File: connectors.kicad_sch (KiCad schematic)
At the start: 9 parts

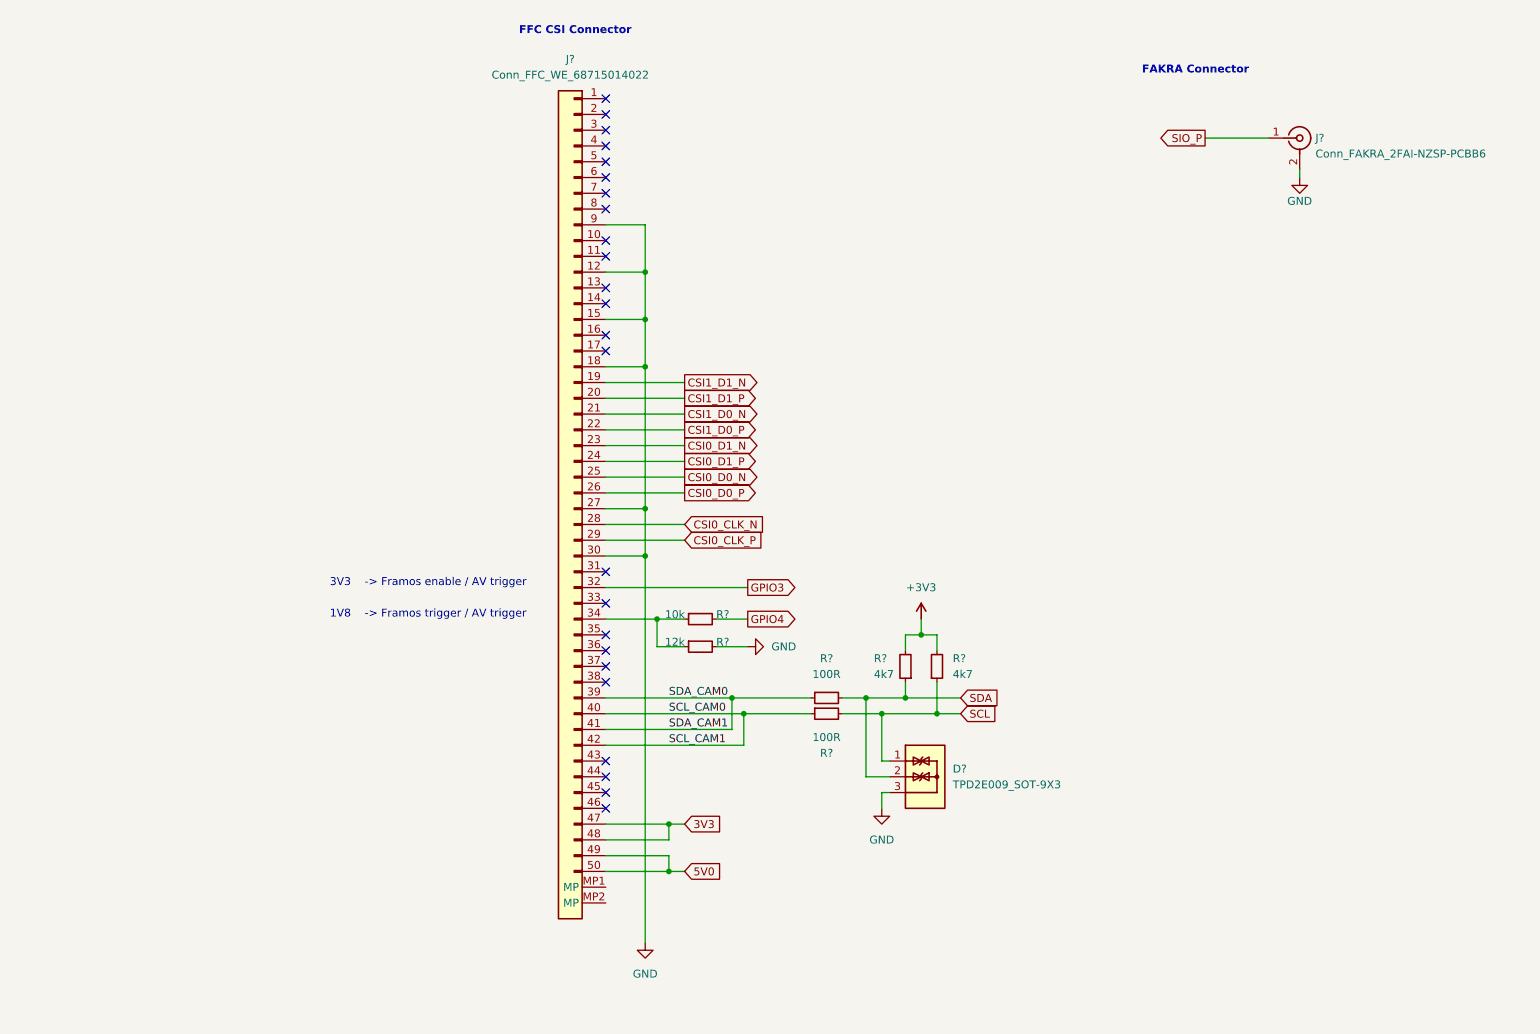
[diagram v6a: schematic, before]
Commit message: Anotate components and fix ERC errors and warnings
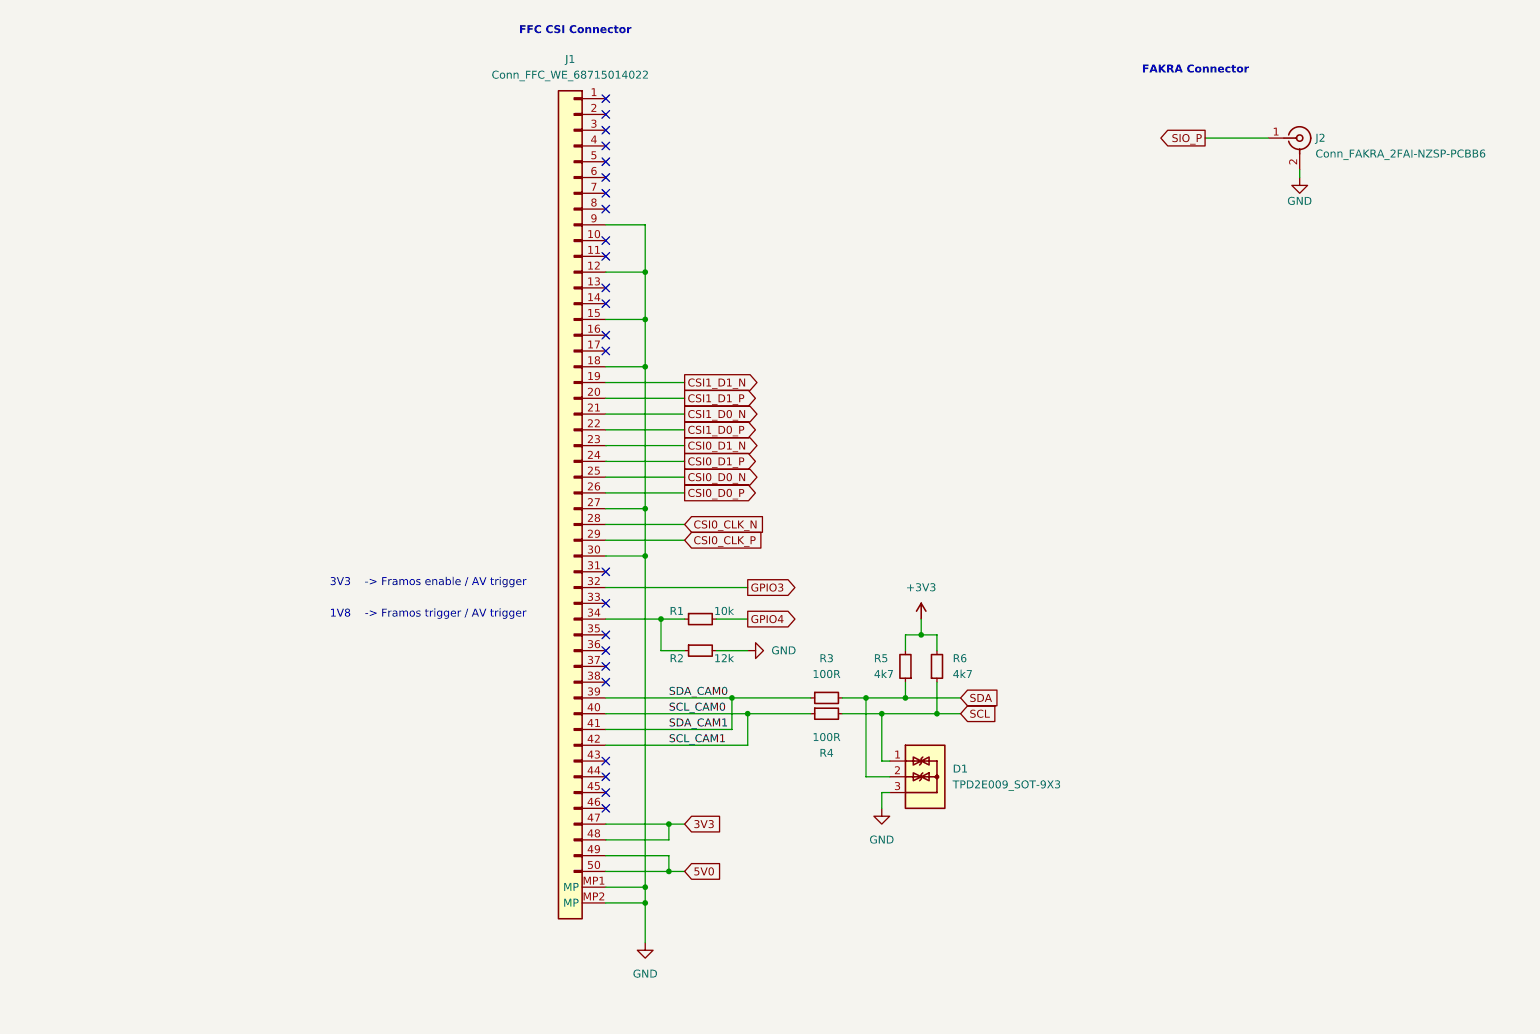
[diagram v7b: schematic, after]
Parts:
- removed R?: R_10k_0402, framos-csi-adapter-footprints:R_0402_1005Metric, symbol framos-csi-adapter:R_10k_0402
- removed R?: R_12k_0402, framos-csi-adapter-footprints:R_0402_1005Metric, symbol framos-csi-adapter:R_12k_0402
- added R1: R_10k_0402, antmicro-footprints:R_0402_1005Metric, symbol antmicroResistors0402:R_10k_0402
- added R2: R_12k_0402, antmicro-footprints:R_0402_1005Metric, symbol antmicroResistors0402:R_12k_0402
- gave numbers to parts that had none: 7
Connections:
- net GND: now also J1.MP1 (MP), J1.MP2 (MP), R2.2
- net GPIO4: now also R1.2
- net at J1.34: now also R1.1, R2.1

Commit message: Implement changes suggested in design review to schematics
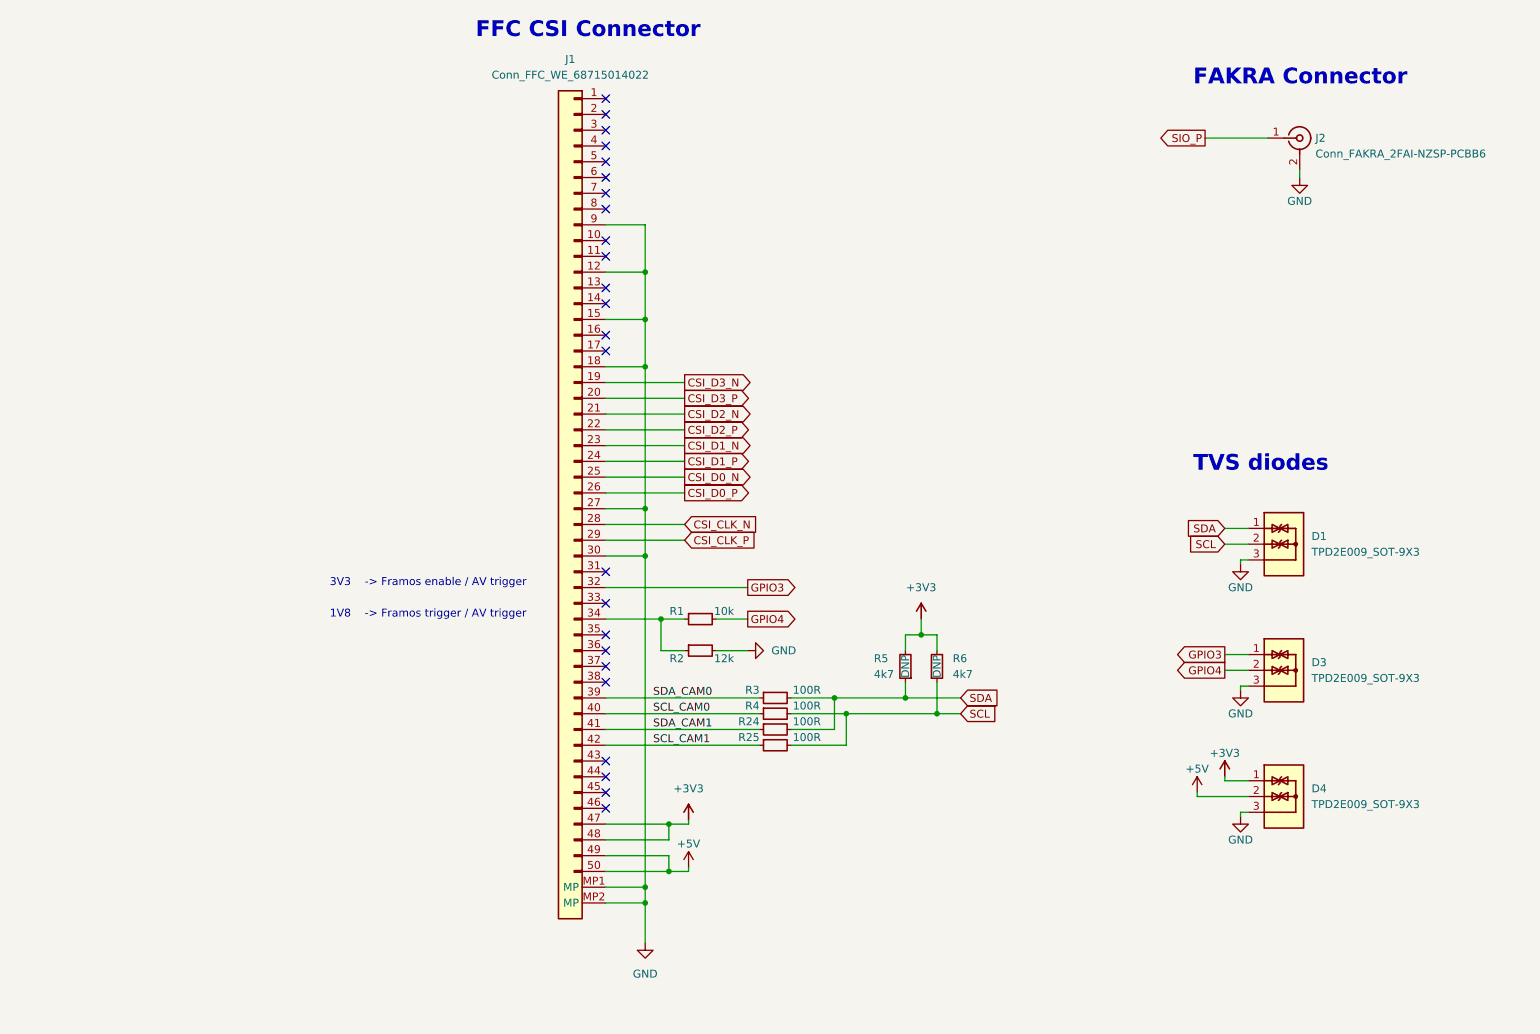
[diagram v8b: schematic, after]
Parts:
- added D3, D4: TPD2E009_SOT-9X3, antmicro-footprints:SOT-723, symbol antmicroTVSDiodes:TPD2E009_SOT-9X3
- added R24, R25: R_100R_0402, antmicro-footprints:R_0402_1005Metric, symbol antmicroResistors0402:R_100R_0402
- R5, R6: DNP (none) -> DNP; now left out of the parts list
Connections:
- net 3V3 is gone; now on net +3V3: J1.47, J1.48
- net +3V3: now also D4.1
- net GND: now also D3.3, D4.3
- net GPIO3: now also D3.1
- net GPIO4: now also D3.2
- net SCL: now also D1.2, R25.2; no longer D1.1
- net SCL_CAM0: no longer J1.42
- net SDA: now also D1.1, R24.2; no longer D1.2
- net SDA_CAM0: no longer J1.41
- net 5V0 renamed +5V
- net +5V: now also D4.2
- net CSI0_CLK_N renamed CSI_CLK_N
- net CSI0_CLK_P renamed CSI_CLK_P
- net CSI0_D0_N renamed CSI_D0_N
- net CSI0_D0_P renamed CSI_D0_P
- net CSI0_D1_N renamed CSI_D1_N
- net CSI0_D1_P renamed CSI_D1_P
- net CSI1_D0_N renamed CSI_D2_N
- net CSI1_D0_P renamed CSI_D2_P
- net CSI1_D1_N renamed CSI_D3_N
- net CSI1_D1_P renamed CSI_D3_P
- new net SCL_CAM1: J1.42, R25.1
- new net SDA_CAM1: J1.41, R24.1
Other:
- note added: "TVS diodes"
- moved on the sheet: R3, R4
